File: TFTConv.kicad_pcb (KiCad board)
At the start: 2 copper layers, 28.8 x 61.2 mm, 5 parts, among them J1 Board, J2 Screen, J3 Conn_01x02_Female, J4 Conn_01x02_Female, J5 Conn_01x02_Female

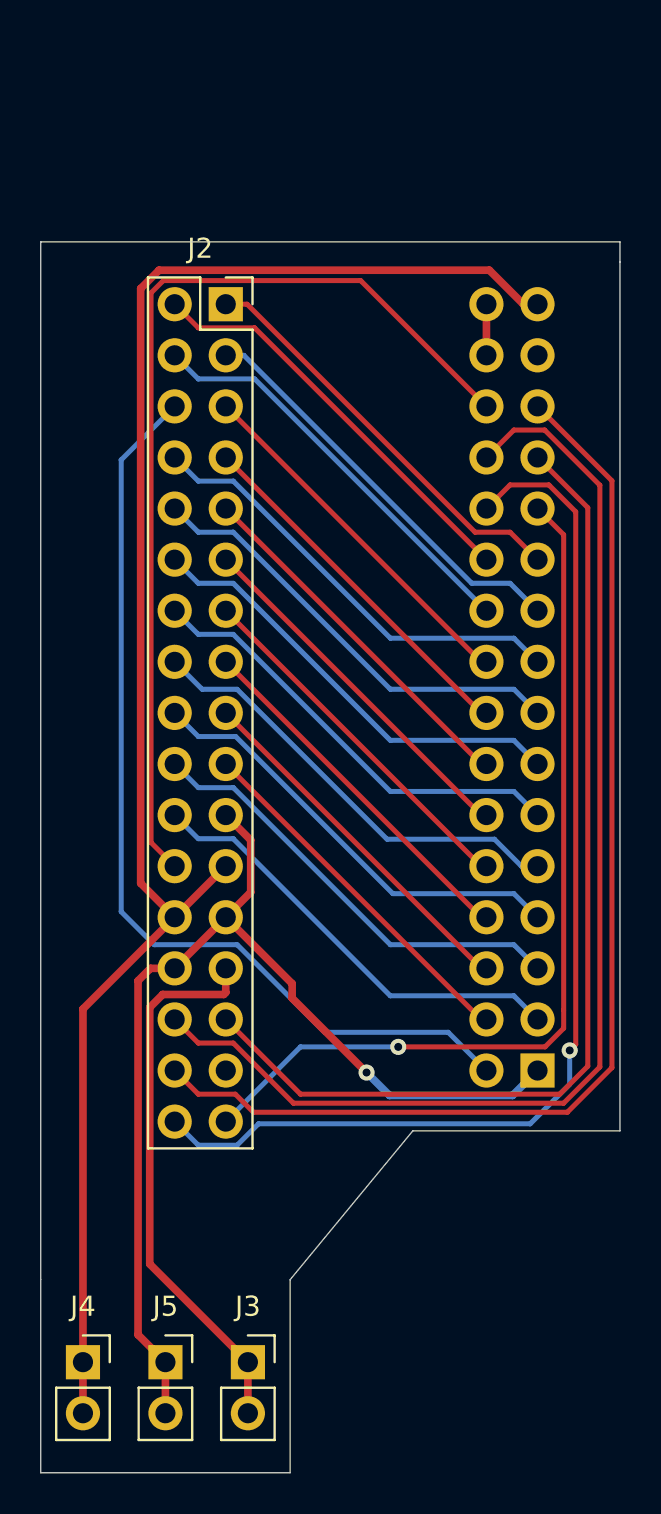
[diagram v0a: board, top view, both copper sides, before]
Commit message: TFTConv: Optimize
Silk, bus length and edge
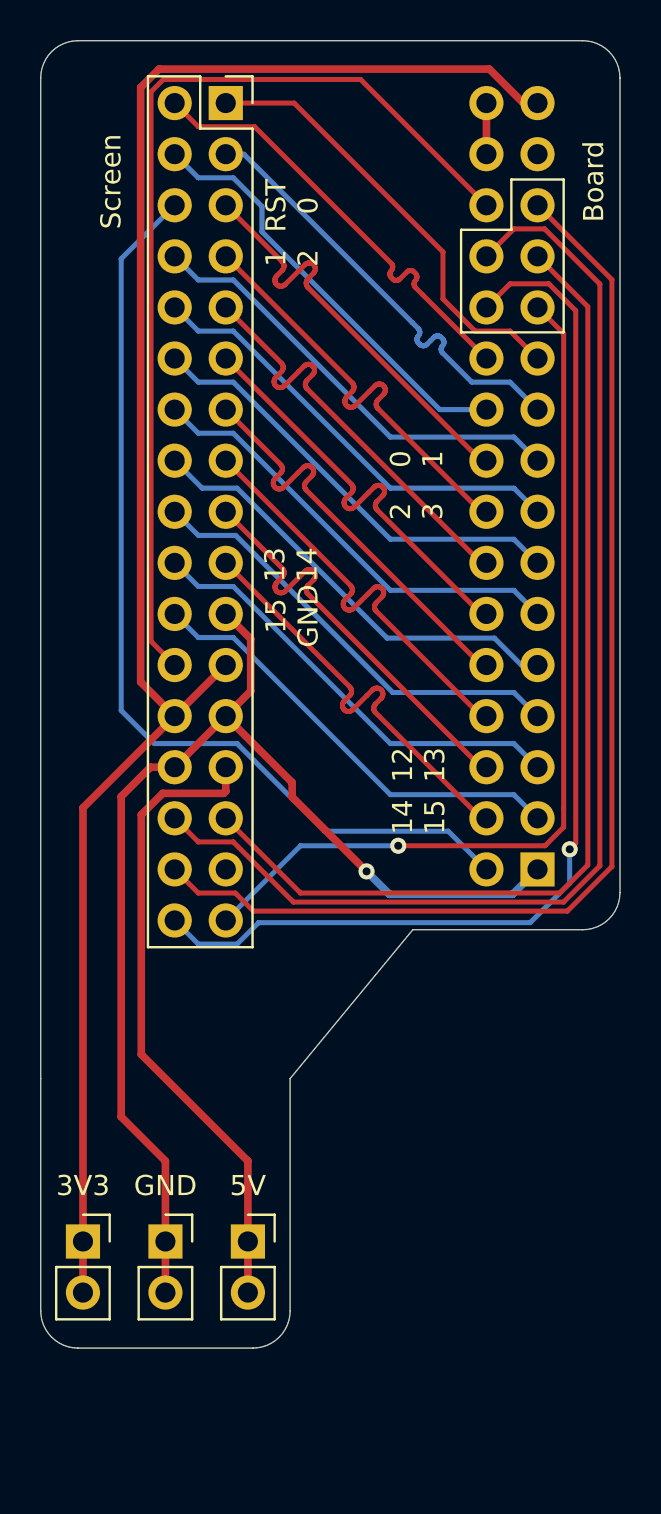
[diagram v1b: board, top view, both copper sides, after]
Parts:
- removed J1: Board, Connector_PinSocket_2.54mm:PinSocket_2x16_P2.54mm_Vertical
- removed J2: Screen, Connector_PinSocket_2.54mm:PinSocket_2x17_P2.54mm_Vertical
- removed J3, J4, J5: Conn_01x02_Female, Connector_PinSocket_2.54mm:PinSocket_1x02_P2.54mm_Vertical
- added 3V3: Conn_01x02_Female, Connector_PinSocket_2.54mm:PinSocket_1x02_P2.54mm_Vertical, F.Cu at (171.6, 125.7)
- added 5V: Conn_01x02_Female, Connector_PinSocket_2.54mm:PinSocket_1x02_P2.54mm_Vertical, F.Cu at (179.8, 125.7)
- added Board: Board, Connector_PinSocket_2.54mm:PinSocket_2x16_P2.54mm_Vertical, B.Cu at (194.2, 107.2)
- added GND: Conn_01x02_Female, Connector_PinSocket_2.54mm:PinSocket_1x02_P2.54mm_Vertical, F.Cu at (175.7, 125.7)
- added Screen: Screen, Connector_PinSocket_2.54mm:PinSocket_2x17_P2.54mm_Vertical, F.Cu at (178.7, 69.1)
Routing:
- net GND: track 53.9 -> 58.6 mm
- net +5V: track 27.5 -> 31.8 mm
- net +3V3: track 82.9 -> 86.9 mm
- net /FSMC_D14: track 18.2 -> 21.4 mm
- net /FSMC_D8: track 18.2 -> 21.4 mm
- net /FSMC_D2: track 18.2 -> 21.4 mm
- net /FSMC_D4: track 18.2 -> 21.4 mm
- net /FSMC_D6: track 18.2 -> 21.4 mm
- net /FSMC_D0: track 18.2 -> 21.4 mm
- net /FSMC_D12: track 18.2 -> 21.4 mm
- net /FSMC_D10: track 18.2 -> 21.4 mm
- net /FSMC_Ax: track 20.8 -> 22.1 mm
- net /FSMC_NEx: track 20.8 -> 22.1 mm
- net /FSMC_NOE: track 20.8 -> 22.1 mm
- net /FSMC_NWE: track 20.8 -> 21.5 mm
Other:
- board size 28.8 x 61.2 mm -> 28.8 x 65 mm
- board text added: "0"
- board text added: "1"
- board text added: "12"
- board text added: "13"
- board text added: "14"
- board text added: "15"
- board text added: "2"
- board text added: "3"
- board text added: "GND"
- board text added: "RST"
